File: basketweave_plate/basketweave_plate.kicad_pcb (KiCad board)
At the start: 2 copper layers, 371.5 x 119.1 mm, 1 part

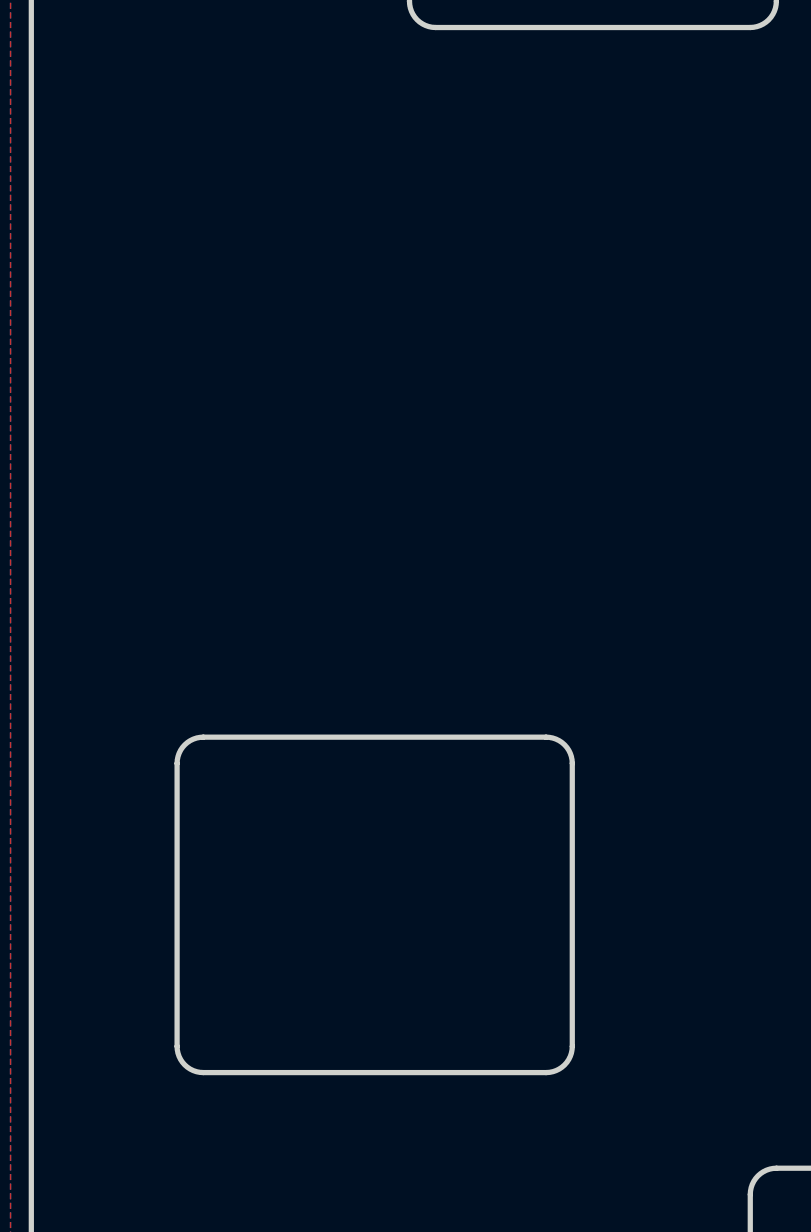
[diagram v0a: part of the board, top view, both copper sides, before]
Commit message: Make macro keys symmetric on both sides; move encoder to the left
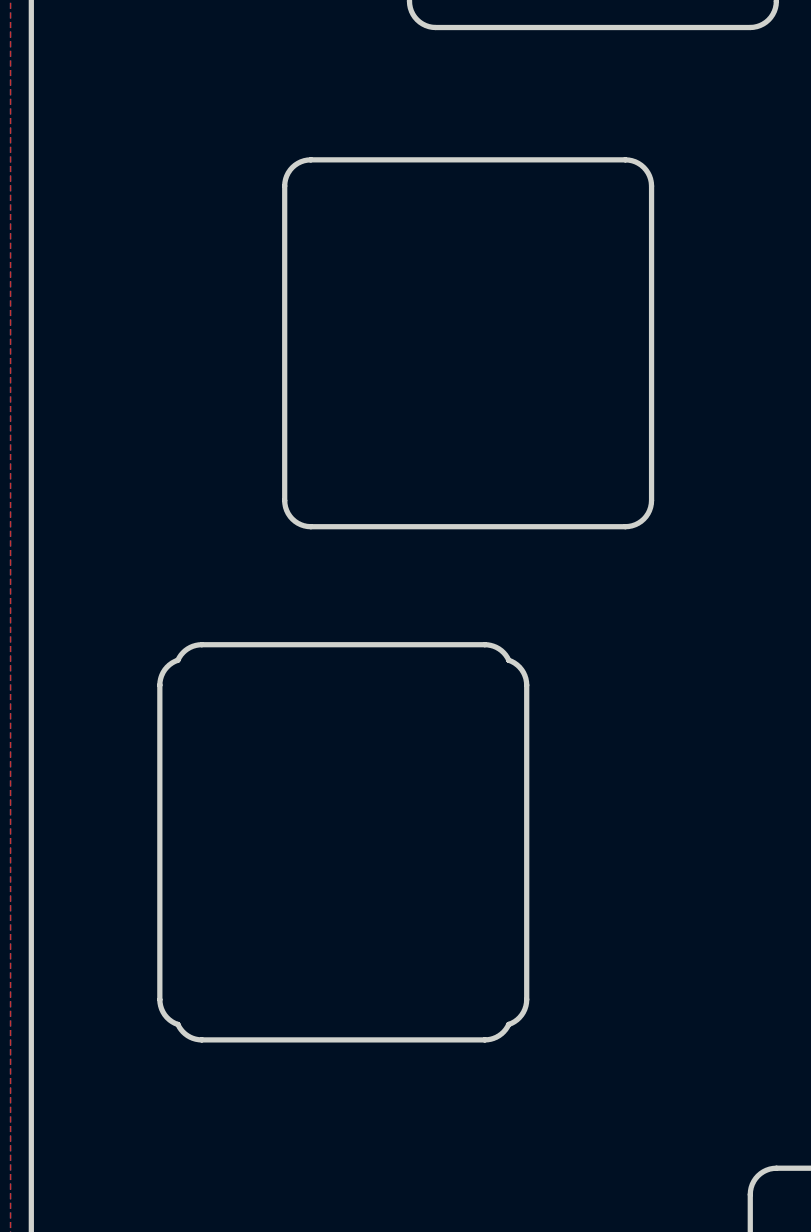
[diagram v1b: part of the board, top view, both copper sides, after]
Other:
- outline, holes or cut-outs redrawn
